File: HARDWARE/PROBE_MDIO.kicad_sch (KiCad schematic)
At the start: 35 parts, among them J1 USB_B_Micro, J2 Conn_01x06_Pin, J3 Conn_02x05_Odd_Even, Q1 2N7002, Q2 2N7002, U1 TXS0102DCU, U2 W25Q32JVZP, U3 SN74LVC1G08DBVR, U4 STM32G474CETx, U5 74LVC74APW.118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

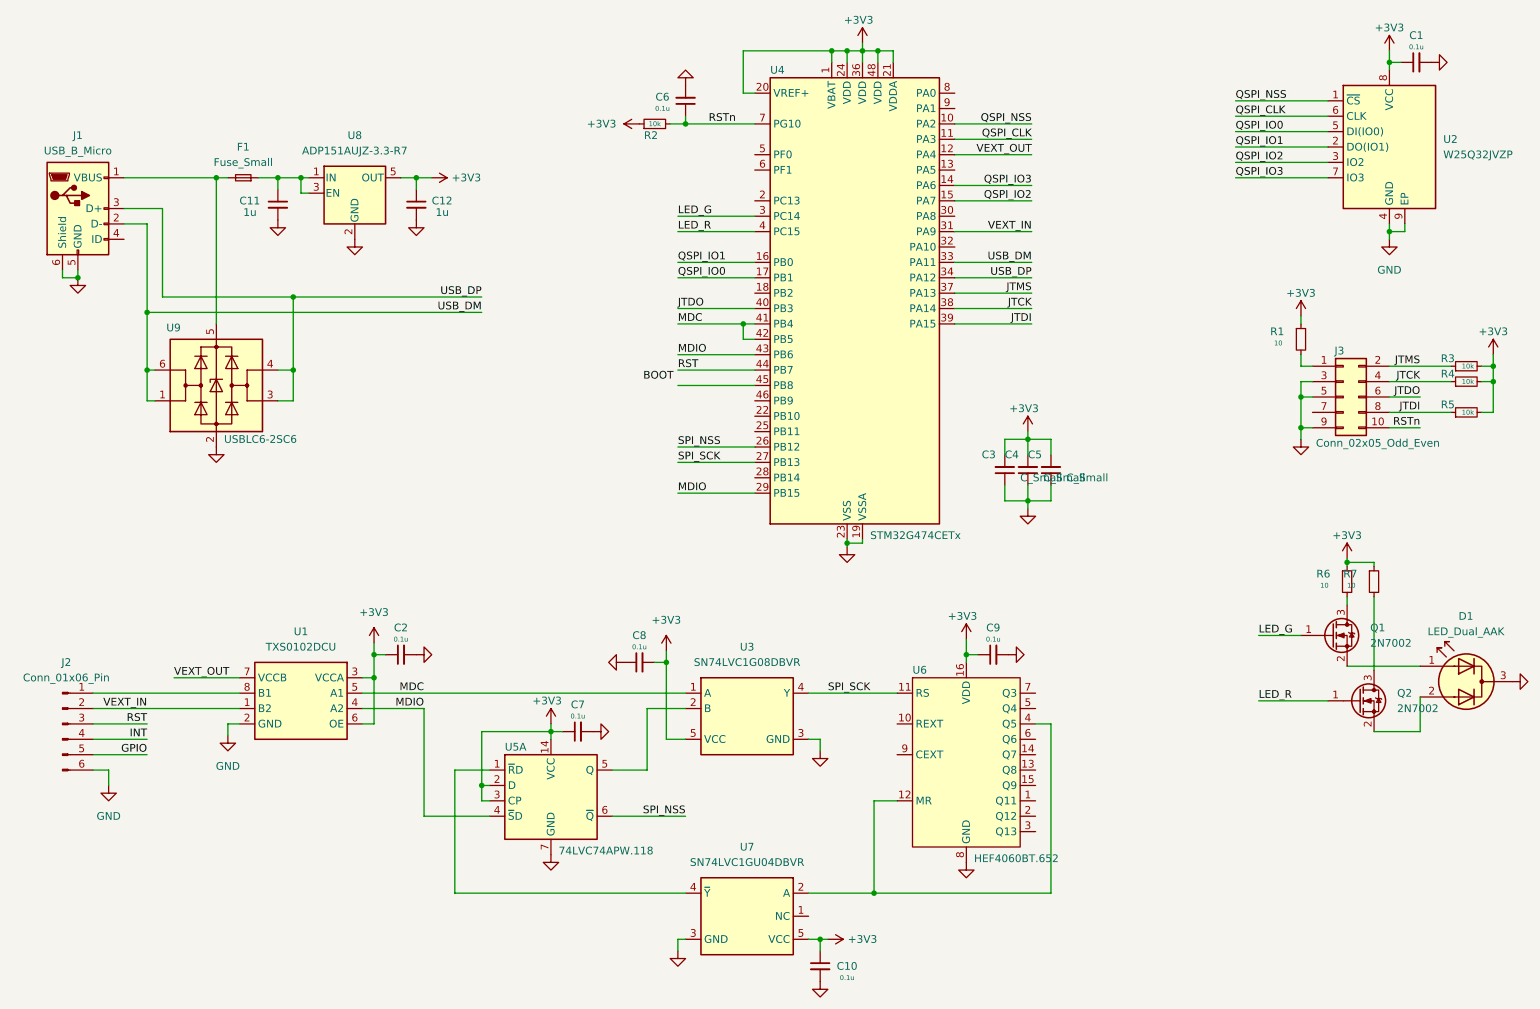
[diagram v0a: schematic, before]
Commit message: Added pcb layout
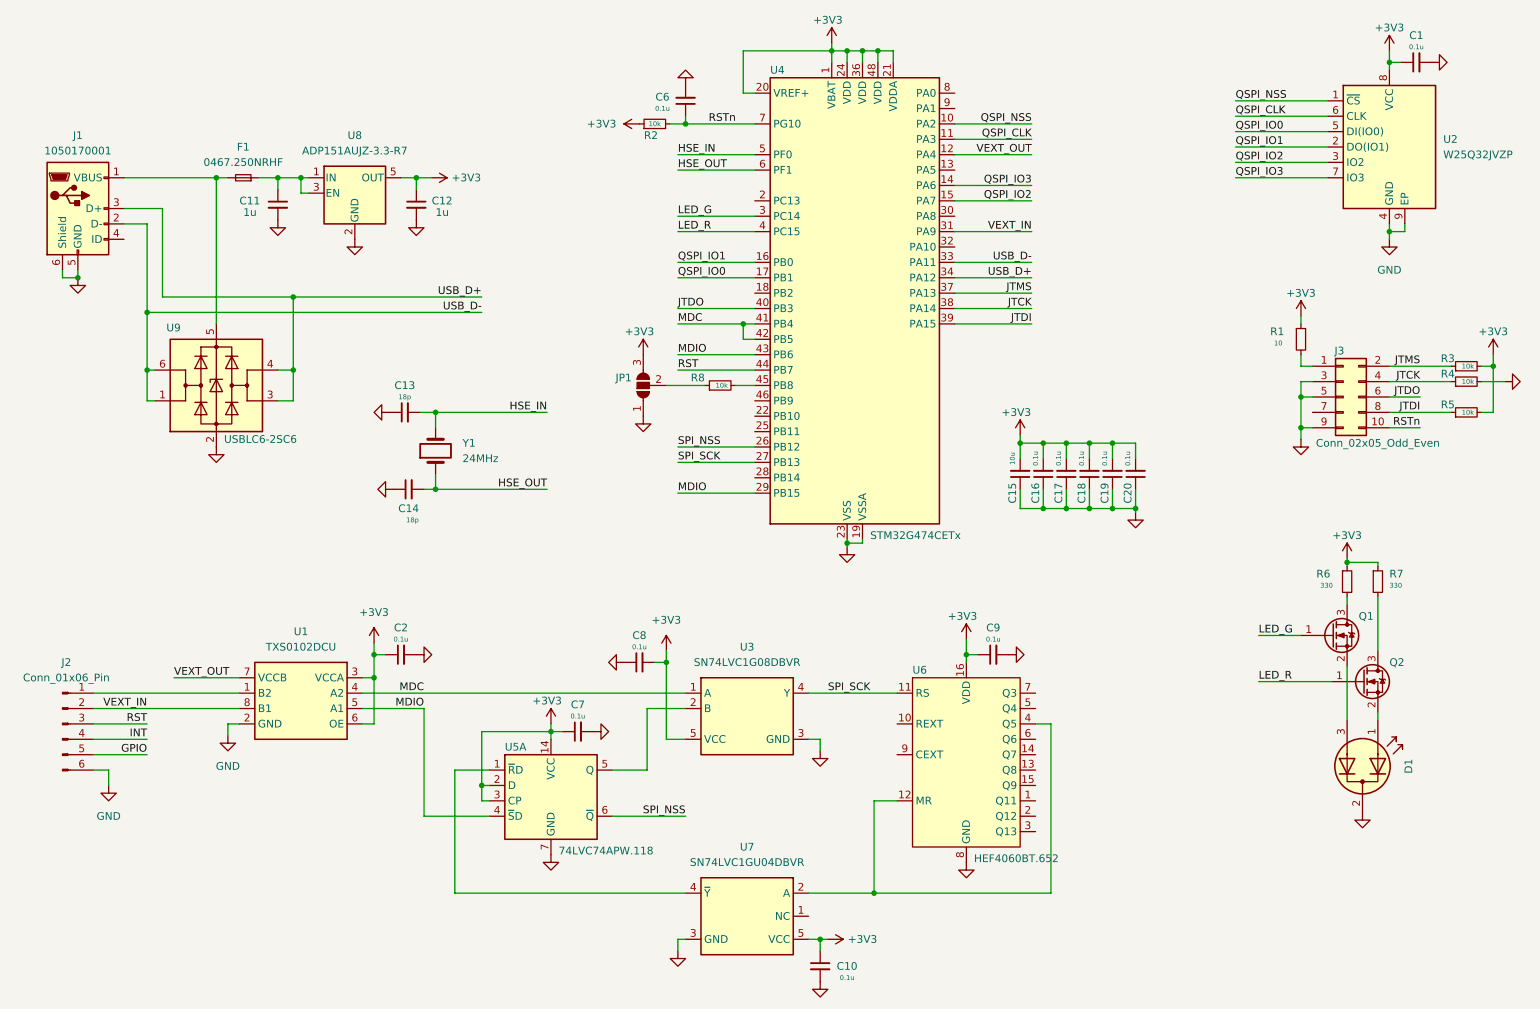
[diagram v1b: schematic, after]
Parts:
- removed C3, C4, C5: C_Small, symbol Device:C_Small
- added C13, C14: 18p, Capacitor_SMD:C_0402_1005Metric, symbol Device:C_Small
- added C15: 10u, Capacitor_SMD:C_0603_1608Metric, symbol Device:C_Small
- added C16, C17, C18, C19, C20: 0.1u, Capacitor_SMD:C_0402_1005Metric, symbol Device:C_Small
- added JP1: SolderJumper_3_Open, Jumper:SolderJumper-3_P2.0mm_Open_TrianglePad1.0x1.5mm_NumberLabels, symbol Jumper:SolderJumper_3_Open
- added R8: 10k, Resistor_SMD:R_0402_1005Metric, symbol Device:R_Small
- added Y1: 24MHz, Crystal:Crystal_SMD_3225-4Pin_3.2x2.5mm, symbol Device:Crystal
- D1: footprint (none) -> LED_THT:LED_D3.0mm-3
- F1: value Fuse_Small -> 0467.250NRHF; footprint (none) -> Fuse:Fuse_0603_1608Metric
- J1: value USB_B_Micro -> 1050170001; footprint FootLIB:USB_Micro-B_MG-10-012 -> Connector_USB:USB_Micro-B_Molex-105017-0001
- J2: footprint (none) -> Connector_PinHeader_2.54mm:PinHeader_1x06_P2.54mm_Horizontal
- J3: footprint (none) -> Connector_PinHeader_1.27mm:PinHeader_2x05_P1.27mm_Vertical
- R1, R3, R4, R5: footprint (none) -> Resistor_SMD:R_0402_1005Metric
- R6, R7: value 10 -> 330; footprint (none) -> Resistor_SMD:R_0402_1005Metric
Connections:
- net +3V3: now also C15.2, C16.2, C17.2, C18.2, C19.2, C20.2, JP1.3 (B); no longer R4.2
- net GND: now also D1.2 (K), R4.2, C13.1, C14.1, C15.1, C16.1, C17.1, C18.1, C19.1, C20.1, JP1.1 (A); no longer D1.3 (K)
- net MDC: now also U1.4 (A2); no longer U1.5 (A1)
- net MDIO: now also U1.5 (A1); no longer U1.4 (A2)
- net VEXT_IN: now also U1.8 (B1); no longer U1.1 (B2)
- net at J2.1 (Pin_1): now also U1.1 (B2); no longer U1.8 (B1)
- net at Q2.2 (S): now also D1.1 (A1); no longer D1.2 (A2)
- net at Q1.2 (S): now also D1.3 (A2); no longer D1.1 (A1)
- net at U4.45 (PB8): now also R8.2
- net HSE_IN: now reaches U4.5 (PF0)
- net HSE_IN: now also C13.2, Y1.3
- net HSE_OUT: now reaches U4.6 (PF1)
- net HSE_OUT: now also C14.2, Y1.1
- net USB_DM renamed USB_D-
- net USB_DP renamed USB_D+
- new net: JP1.2 (C), R8.1
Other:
- moved on the sheet: D1, Q2, R7
